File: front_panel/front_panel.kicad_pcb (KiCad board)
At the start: 2 copper layers, 68.8 x 19.8 mm, 0 parts

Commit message: DC current symbol
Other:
- board text added: "POWER ONLY 5V⎓500mA"
- board text removed: "POWER ONLY 5V/500mA"
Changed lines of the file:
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@@
 		(layer "Edge.Cuts")
 	)
-	(gr_text "POWER ONLY\n5V/500mA"
+	(gr_text "POWER ONLY\n5V⎓500mA"
 		(at 110.9 107.15 0)
 		(layer "F.SilkS")

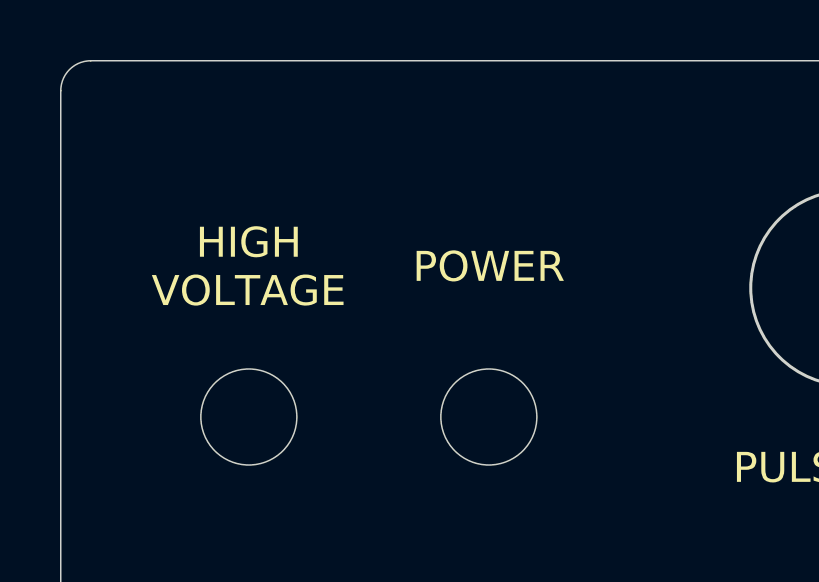
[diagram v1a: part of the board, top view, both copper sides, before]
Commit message: Swap LEDs, update 3D models
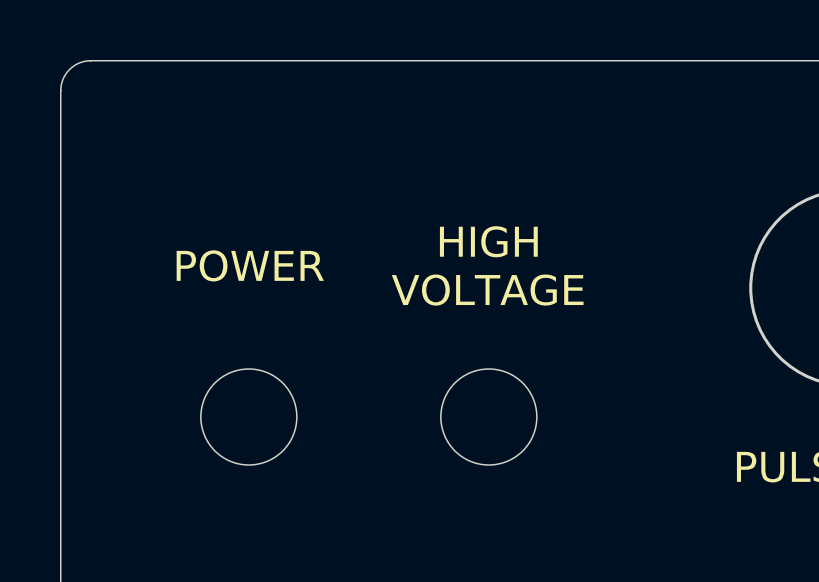
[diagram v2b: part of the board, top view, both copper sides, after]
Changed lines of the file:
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@@
 	)
 	(gr_text "HIGH\nVOLTAGE"
-		(at 71.895 96.95 0)
+		(at 79.895 96.95 0)
 		(layer "F.SilkS")
 		(effects
@@
 	)
 	(gr_text "POWER"
-		(at 79.895 96.95 0)
+		(at 71.895 96.95 0)
 		(layer "F.SilkS")
 		(effects
